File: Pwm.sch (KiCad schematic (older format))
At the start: 15 parts, among them P4 CONN_01X03, P5 CONN_01X03, P6 CONN_01X03, P7 CONN_01X03, U6 PCA9551

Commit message: version preliminar de la etapa de alimentacion
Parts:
- renumbered C7 to C21, C8 to C22, C9 to C23, C10 to C24, C11 to C25, P4 to P2, P5 to P3, P6 to P4, P7 to P5, R15 to R16, R16 to R17, R17 to R18, R18 to R19, R19 to R20, U6 to U9
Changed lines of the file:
@@
 LIBS:Sensores
 LIBS:Reles
+LIBS:Reguladores
+LIBS:Transistores
 LIBS:Wifi_PB-cache
 EELAYER 26 0
@@
 $Descr User 8268 5846
 encoding utf-8
-Sheet 7 11
+Sheet 7 15
 Title "Puerto de expansión para servomotores"
 Date "2017-01-15"
@@
 $EndDescr
 $Comp
-L CONN_01X03 P4
+L CONN_01X03 P2
 U 1 1 5794EA47
 P 6550 1350
-F 0 "P4" H 6628 1391 50  0000 L CNN
+F 0 "P2" H 6628 1391 50  0000 L CNN
 F 1 "CONN_01X03" H 6628 1300 50  0000 L CNN
 F 2 "Pin_Headers:Pin_Header_Straight_1x03_Pitch2.54mm" H 6550 1350 50  0001 C CNN
@@
 $EndComp
 $Comp
-L CONN_01X03 P5
+L CONN_01X03 P3
 U 1 1 5794EAA8
 P 6550 2050
-F 0 "P5" H 6628 2091 50  0000 L CNN
+F 0 "P3" H 6628 2091 50  0000 L CNN
 F 1 "CONN_01X03" H 6628 2000 50  0000 L CNN
 F 2 "Pin_Headers:Pin_Header_Straight_1x03_Pitch2.54mm" H 6550 2050 50  0001 C CNN
@@
 $EndComp
 $Comp
-L +5V #PWR026
+L +5V #PWR64
 U 1 1 5794EAD6
 P 6100 750
-F 0 "#PWR026" H 6100 600 50  0001 C CNN
+F 0 "#PWR64" H 6100 600 50  0001 C CNN
 F 1 "+5V" H 6115 923 50  0000 C CNN
 F 2 "" H 6100 750 50  0000 C CNN
@@
 $EndComp
 $Comp
-L GND #PWR027
+L GND #PWR65
 U 1 1 5794EAEE
 P 6200 3850
-F 0 "#PWR027" H 6200 3600 50  0001 C CNN
+F 0 "#PWR65" H 6200 3600 50  0001 C CNN
 F 1 "GND" H 6205 3677 50  0000 C CNN
 F 2 "" H 6200 3850 50  0000 C CNN
@@
 $EndBitmap
 $Comp
-L PCA9551 U6
+L PCA9551 U9
 U 1 1 586D5351
 P 1550 3800
-F 0 "U6" H 2100 3717 60  0000 C CNN
+F 0 "U9" H 2100 3717 60  0000 C CNN
 F 1 "PCA9551" H 2100 3597 79  0000 C CNN
 F 2 "Housings_SSOP:TSSOP-16_4.4x5mm_Pitch0.65mm" H 1550 3930 60  0001 C CNN
@@
 $EndComp
 $Comp
-L CONN_01X03 P6
+L CONN_01X03 P4
 U 1 1 586D53FE
 P 6550 2750
-F 0 "P6" H 6628 2791 50  0000 L CNN
+F 0 "P4" H 6628 2791 50  0000 L CNN
 F 1 "CONN_01X03" H 6628 2700 50  0000 L CNN
 F 2 "Pin_Headers:Pin_Header_Straight_1x03_Pitch2.54mm" H 6550 2750 50  0001 C CNN
@@
 $EndComp
 $Comp
-L CONN_01X03 P7
+L CONN_01X03 P5
 U 1 1 586D547C
 P 6550 3450
-F 0 "P7" H 6628 3491 50  0000 L CNN
+F 0 "P5" H 6628 3491 50  0000 L CNN
 F 1 "CONN_01X03" H 6628 3400 50  0000 L CNN
 F 2 "Pin_Headers:Pin_Header_Straight_1x03_Pitch2.54mm" H 6550 3450 50  0001 C CNN
@@
 	4100 1200 4100 1000
 $Comp
-L +5V #PWR028
+L +5V #PWR58
 U 1 1 586D5A4A
 P 4100 1000
-F 0 "#PWR028" H 4100 850 50  0001 C CNN
+F 0 "#PWR58" H 4100 850 50  0001 C CNN
 F 1 "+5V" H 4115 1173 50  0000 C CNN
 F 2 "" H 4100 1000 50  0000 C CNN
@@
 $EndComp
 $Comp
-L +5V #PWR029
+L +5V #PWR56
 U 1 1 586D5A77
 P 3750 1000
-F 0 "#PWR029" H 3750 850 50  0001 C CNN
+F 0 "#PWR56" H 3750 850 50  0001 C CNN
 F 1 "+5V" H 3765 1173 50  0000 C CNN
 F 2 "" H 3750 1000 50  0000 C CNN
@@
 $EndComp
 $Comp
-L +5V #PWR030
+L +5V #PWR54
 U 1 1 586D5A9D
 P 3400 1000
-F 0 "#PWR030" H 3400 850 50  0001 C CNN
+F 0 "#PWR54" H 3400 850 50  0001 C CNN
 F 1 "+5V" H 3415 1173 50  0000 C CNN
 F 2 "" H 3400 1000 50  0000 C CNN
@@
 $EndComp
 $Comp
-L +5V #PWR031
+L +5V #PWR52
 U 1 1 586D5AC3
 P 3050 1000
-F 0 "#PWR031" H 3050 850 50  0001 C CNN
+F 0 "#PWR52" H 3050 850 50  0001 C CNN
 F 1 "+5V" H 3065 1173 50  0000 C CNN
 F 2 "" H 3050 1000 50  0000 C CNN
@@
 $EndComp
 $Comp
-L GND #PWR032
+L GND #PWR53
 U 1 1 586D5AE2
 P 3050 1750
-F 0 "#PWR032" H 3050 1500 50  0001 C CNN
+F 0 "#PWR53" H 3050 1500 50  0001 C CNN
 F 1 "GND" H 3055 1577 50  0000 C CNN
 F 2 "" H 3050 1750 50  0000 C CNN
@@
 $EndComp
 $Comp
-L GND #PWR033
+L GND #PWR55
 U 1 1 586D5B0F
 P 3400 1750
-F 0 "#PWR033" H 3400 1500 50  0001 C CNN
+F 0 "#PWR55" H 3400 1500 50  0001 C CNN
 F 1 "GND" H 3405 1577 50  0000 C CNN
 F 2 "" H 3400 1750 50  0000 C CNN
@@
 $EndComp
 $Comp
-L GND #PWR034
+L GND #PWR57
 U 1 1 586D5B35
 P 3750 1750
-F 0 "#PWR034" H 3750 1500 50  0001 C CNN
+F 0 "#PWR57" H 3750 1500 50  0001 C CNN
 F 1 "GND" H 3755 1577 50  0000 C CNN
 F 2 "" H 3750 1750 50  0000 C CNN
@@
 $EndComp
 $Comp
-L GND #PWR035
+L GND #PWR59
 U 1 1 586D5B5B
 P 4100 1750
-F 0 "#PWR035" H 4100 1500 50  0001 C CNN
+F 0 "#PWR59" H 4100 1500 50  0001 C CNN
 F 1 "GND" H 4105 1577 50  0000 C CNN
 F 2 "" H 4100 1750 50  0000 C CNN
@@
 	2100 1450 2100 2350
 $Comp
-L GND #PWR036
+L GND #PWR51
 U 1 1 586D5DFC
 P 1750 2100
-F 0 "#PWR036" H 1750 1850 50  0001 C CNN
+F 0 "#PWR51" H 1750 1850 50  0001 C CNN
 F 1 "GND" H 1755 1927 50  0000 C CNN
 F 2 "" H 1750 2100 50  0000 C CNN
@@
 	1200 3250 1200 3950
 $Comp
-L GND #PWR037
+L GND #PWR49
 U 1 1 586D660B
 P 1200 3950
-F 0 "#PWR037" H 1200 3700 50  0001 C CNN
+F 0 "#PWR49" H 1200 3700 50  0001 C CNN
 F 1 "GND" H 1205 3777 50  0000 C CNN
 F 2 "" H 1200 3950 50  0000 C CNN
@@
 SERVO4
 $Comp
-L +5V #PWR038
+L +5V #PWR50
 U 1 1 586D839D
 P 1750 1300
-F 0 "#PWR038" H 1750 1150 50  0001 C CNN
+F 0 "#PWR50" H 1750 1150 50  0001 C CNN
 F 1 "+5V" H 1765 1473 50  0000 C CNN
 F 2 "" H 1750 1300 50  0000 C CNN
@@
 	5600 800  5600 850
 $Comp
-L +5V #PWR039
+L +5V #PWR63
 U 1 1 586FF4A2
 P 5600 2900
-F 0 "#PWR039" H 5600 2750 50  0001 C CNN
+F 0 "#PWR63" H 5600 2750 50  0001 C CNN
 F 1 "+5V" H 5615 3073 50  0000 C CNN
 F 2 "" H 5600 2900 50  0000 C CNN
@@
 	5600 2900 5600 2950
 $Comp
-L +5V #PWR040
+L +5V #PWR60
 U 1 1 586FF5CA
 P 5600 800
-F 0 "#PWR040" H 5600 650 50  0001 C CNN
+F 0 "#PWR60" H 5600 650 50  0001 C CNN
 F 1 "+5V" H 5615 973 50  0000 C CNN
 F 2 "" H 5600 800 50  0000 C CNN
@@
 $EndComp
 $Comp
-L +5V #PWR041
+L +5V #PWR62
 U 1 1 586FF689
 P 5600 2200
-F 0 "#PWR041" H 5600 2050 50  0001 C CNN
+F 0 "#PWR62" H 5600 2050 50  0001 C CNN
 F 1 "+5V" H 5615 2373 50  0000 C CNN
 F 2 "" H 5600 2200 50  0000 C CNN
@@
 $EndComp
 $Comp
-L +5V #PWR042
+L +5V #PWR61
 U 1 1 586FF6C1
 P 5600 1500
-F 0 "#PWR042" H 5600 1350 50  0001 C CNN
+F 0 "#PWR61" H 5600 1350 50  0001 C CNN
 F 1 "+5V" H 5615 1673 50  0000 C CNN
 F 2 "" H 5600 1500 50  0000 C CNN
@@
 	750  3050 1350 3050
 $Comp
-L +5V #PWR043
+L +5V #PWR48
 U 1 1 58700007
 P 750 2450
-F 0 "#PWR043" H 750 2300 50  0001 C CNN
+F 0 "#PWR48" H 750 2300 50  0001 C CNN
 F 1 "+5V" H 765 2623 50  0000 C CNN
 F 2 "" H 750 2450 50  0000 C CNN
@@
 	750  2450 750  2600
 $Comp
-L R R15
+L R R16
 U 1 1 58700C10
 P 750 2750
-F 0 "R15" V 850 2650 50  0000 L CNN
+F 0 "R16" V 850 2650 50  0000 L CNN
 F 1 "10K" V 750 2650 50  0000 L CNN
 F 2 "Resistencias:R_0805" V 680 2750 50  0001 C CNN
@@
 $EndComp
 $Comp
-L R R19
+L R R20
 U 1 1 58700D4F
 P 5600 3100
-F 0 "R19" V 5700 3000 50  0000 L CNN
+F 0 "R20" V 5700 3000 50  0000 L CNN
 F 1 "10K" V 5600 3000 50  0000 L CNN
 F 2 "Resistencias:R_0805" V 5530 3100 50  0001 C CNN
@@
 $EndComp
 $Comp
-L R R18
+L R R19
 U 1 1 58700ECF
 P 5600 2400
-F 0 "R18" V 5700 2300 50  0000 L CNN
+F 0 "R19" V 5700 2300 50  0000 L CNN
 F 1 "10K" V 5600 2300 50  0000 L CNN
 F 2 "Resistencias:R_0805" V 5530 2400 50  0001 C CNN
@@
 $EndComp
 $Comp
-L R R16
+L R R17
 U 1 1 5870102D
 P 5600 1000
-F 0 "R16" V 5700 900 50  0000 L CNN
+F 0 "R17" V 5700 900 50  0000 L CNN
 F 1 "10K" V 5600 900 50  0000 L CNN
 F 2 "Resistencias:R_0805" V 5530 1000 50  0001 C CNN
@@
 $EndComp
 $Comp
-L R R17
+L R R18
 U 1 1 5870117D
 P 5600 1700
-F 0 "R17" V 5700 1600 50  0000 L CNN
+F 0 "R18" V 5700 1600 50  0000 L CNN
 F 1 "10K" V 5600 1600 50  0000 L CNN
 F 2 "Resistencias:R_0805" V 5530 1700 50  0001 C CNN
@@
 	6350 1350 6100 1350
 $Comp
-L C C7
+L C C21
 U 1 1 58701807
 P 1750 1800
-F 0 "C7" H 1775 1900 50  0000 L CNN
+F 0 "C21" H 1775 1900 50  0000 L CNN
 F 1 "100n" H 1775 1700 50  0000 L CNN
 F 2 "Capacitors_SMD:C_0805" H 1788 1650 50  0001 C CNN
@@
 $EndComp
 $Comp
-L C C8
+L C C22
 U 1 1 58701B7E
 P 3050 1350
-F 0 "C8" H 3165 1396 50  0000 L CNN
+F 0 "C22" H 3165 1396 50  0000 L CNN
 F 1 "1u" H 3165 1305 50  0000 L CNN
 F 2 "Capacitors_SMD:C_0805" H 3088 1200 50  0001 C CNN
@@
 $EndComp
 $Comp
-L C C9
+L C C23
 U 1 1 58701CA2
 P 3400 1350
-F 0 "C9" H 3515 1396 50  0000 L CNN
+F 0 "C23" H 3515 1396 50  0000 L CNN
 F 1 "1u" H 3515 1305 50  0000 L CNN
 F 2 "Capacitors_SMD:C_0805" H 3438 1200 50  0001 C CNN
@@
 $EndComp
 $Comp
-L C C10
+L C C24
 U 1 1 58701CFA
 P 3750 1350
-F 0 "C10" H 3865 1396 50  0000 L CNN
+F 0 "C24" H 3865 1396 50  0000 L CNN
 F 1 "1u" H 3865 1305 50  0000 L CNN
 F 2 "Capacitors_SMD:C_0805" H 3788 1200 50  0001 C CNN
@@
 $EndComp
 $Comp
-L C C11
+L C C25
 U 1 1 58701D4D
 P 4100 1350
-F 0 "C11" H 4215 1396 50  0000 L CNN
+F 0 "C25" H 4215 1396 50  0000 L CNN
 F 1 "1u" H 4215 1305 50  0000 L CNN
 F 2 "Capacitors_SMD:C_0805" H 4138 1200 50  0001 C CNN

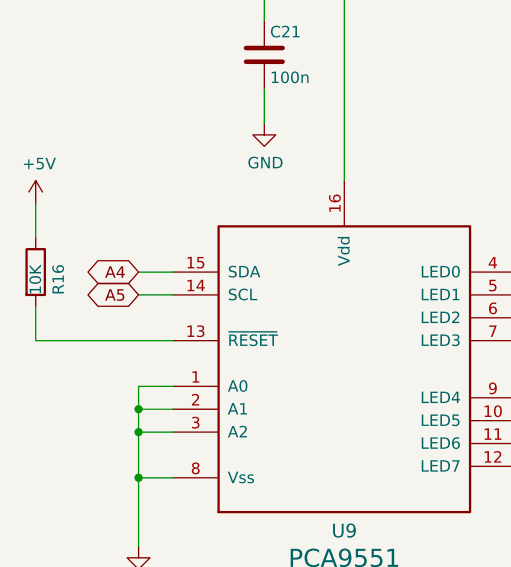
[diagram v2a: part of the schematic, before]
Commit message: cambiar ch340T por ch340g y añadir nc a pines
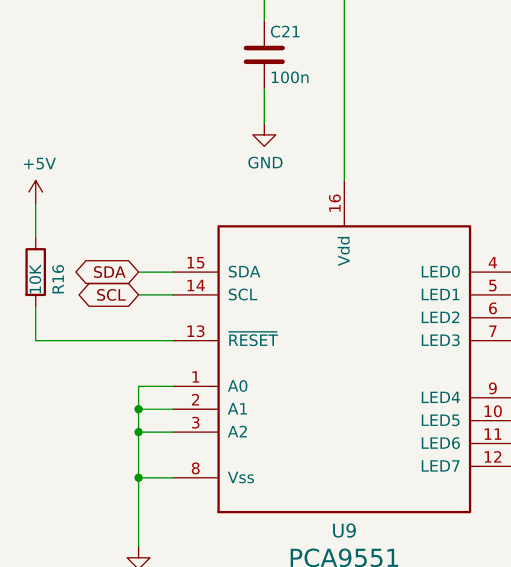
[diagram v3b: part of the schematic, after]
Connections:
- net A4 renamed SDA
- net A5 renamed SCL
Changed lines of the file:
@@
 $Descr User 8268 5846
 encoding utf-8
-Sheet 7 15
+Sheet 7 14
 Title "Puerto de expansión para servomotores"
 Date "2017-01-15"
@@
 $EndComp
 $Comp
-L +5V #PWR062
+L +5V #PWR070
 U 1 1 5794EAD6
 P 6100 750
-F 0 "#PWR062" H 6100 600 50  0001 C CNN
+F 0 "#PWR070" H 6100 600 50  0001 C CNN
 F 1 "+5V" H 6115 923 50  0000 C CNN
 F 2 "" H 6100 750 50  0000 C CNN
@@
 $EndComp
 $Comp
-L GND #PWR063
+L GND #PWR071
 U 1 1 5794EAEE
 P 6200 3850
-F 0 "#PWR063" H 6200 3600 50  0001 C CNN
+F 0 "#PWR071" H 6200 3600 50  0001 C CNN
 F 1 "GND" H 6205 3677 50  0000 C CNN
 F 2 "" H 6200 3850 50  0000 C CNN
@@
 	4100 1200 4100 1000
 $Comp
-L +5V #PWR064
+L +5V #PWR072
 U 1 1 586D5A4A
 P 4100 1000
-F 0 "#PWR064" H 4100 850 50  0001 C CNN
+F 0 "#PWR072" H 4100 850 50  0001 C CNN
 F 1 "+5V" H 4115 1173 50  0000 C CNN
 F 2 "" H 4100 1000 50  0000 C CNN
@@
 $EndComp
 $Comp
-L +5V #PWR065
+L +5V #PWR073
 U 1 1 586D5A77
 P 3750 1000
-F 0 "#PWR065" H 3750 850 50  0001 C CNN
+F 0 "#PWR073" H 3750 850 50  0001 C CNN
 F 1 "+5V" H 3765 1173 50  0000 C CNN
 F 2 "" H 3750 1000 50  0000 C CNN
@@
 $EndComp
 $Comp
-L +5V #PWR066
+L +5V #PWR074
 U 1 1 586D5A9D
 P 3400 1000
-F 0 "#PWR066" H 3400 850 50  0001 C CNN
+F 0 "#PWR074" H 3400 850 50  0001 C CNN
 F 1 "+5V" H 3415 1173 50  0000 C CNN
 F 2 "" H 3400 1000 50  0000 C CNN
@@
 $EndComp
 $Comp
-L +5V #PWR067
+L +5V #PWR075
 U 1 1 586D5AC3
 P 3050 1000
-F 0 "#PWR067" H 3050 850 50  0001 C CNN
+F 0 "#PWR075" H 3050 850 50  0001 C CNN
 F 1 "+5V" H 3065 1173 50  0000 C CNN
 F 2 "" H 3050 1000 50  0000 C CNN
@@
 $EndComp
 $Comp
-L GND #PWR068
+L GND #PWR076
 U 1 1 586D5AE2
 P 3050 1750
-F 0 "#PWR068" H 3050 1500 50  0001 C CNN
+F 0 "#PWR076" H 3050 1500 50  0001 C CNN
 F 1 "GND" H 3055 1577 50  0000 C CNN
 F 2 "" H 3050 1750 50  0000 C CNN
@@
 $EndComp
 $Comp
-L GND #PWR069
+L GND #PWR077
 U 1 1 586D5B0F
 P 3400 1750
-F 0 "#PWR069" H 3400 1500 50  0001 C CNN
+F 0 "#PWR077" H 3400 1500 50  0001 C CNN
 F 1 "GND" H 3405 1577 50  0000 C CNN
 F 2 "" H 3400 1750 50  0000 C CNN
@@
 $EndComp
 $Comp
-L GND #PWR070
+L GND #PWR078
 U 1 1 586D5B35
 P 3750 1750
-F 0 "#PWR070" H 3750 1500 50  0001 C CNN
+F 0 "#PWR078" H 3750 1500 50  0001 C CNN
 F 1 "GND" H 3755 1577 50  0000 C CNN
 F 2 "" H 3750 1750 50  0000 C CNN
@@
 $EndComp
 $Comp
-L GND #PWR071
+L GND #PWR079
 U 1 1 586D5B5B
 P 4100 1750
-F 0 "#PWR071" H 4100 1500 50  0001 C CNN
+F 0 "#PWR079" H 4100 1500 50  0001 C CNN
 F 1 "GND" H 4105 1577 50  0000 C CNN
 F 2 "" H 4100 1750 50  0000 C CNN
@@
 	2100 1450 2100 2350
 $Comp
-L GND #PWR072
+L GND #PWR080
 U 1 1 586D5DFC
 P 1750 2100
-F 0 "#PWR072" H 1750 1850 50  0001 C CNN
+F 0 "#PWR080" H 1750 1850 50  0001 C CNN
 F 1 "GND" H 1755 1927 50  0000 C CNN
 F 2 "" H 1750 2100 50  0000 C CNN
@@
 	1200 3250 1200 3950
 $Comp
-L GND #PWR073
+L GND #PWR081
 U 1 1 586D660B
 P 1200 3950
-F 0 "#PWR073" H 1200 3700 50  0001 C CNN
+F 0 "#PWR081" H 1200 3700 50  0001 C CNN
 F 1 "GND" H 1205 3777 50  0000 C CNN
 F 2 "" H 1200 3950 50  0000 C CNN
@@
 	1350 2750 1200 2750
 Text GLabel 1200 2750 0    50   BiDi ~ 0
-A4
+SDA
 Wire Wire Line
 	1200 2850 1350 2850
 Text GLabel 1200 2850 0    50   BiDi ~ 0
-A5
+SCL
 Text GLabel 3400 3300 2    50   Output ~ 0
 LED_RED
@@
 SERVO4
 $Comp
-L +5V #PWR074
+L +5V #PWR082
 U 1 1 586D839D
 P 1750 1300
-F 0 "#PWR074" H 1750 1150 50  0001 C CNN
+F 0 "#PWR082" H 1750 1150 50  0001 C CNN
 F 1 "+5V" H 1765 1473 50  0000 C CNN
 F 2 "" H 1750 1300 50  0000 C CNN
@@
 	5600 800  5600 850
 $Comp
-L +5V #PWR075
+L +5V #PWR083
 U 1 1 586FF4A2
 P 5600 2900
-F 0 "#PWR075" H 5600 2750 50  0001 C CNN
+F 0 "#PWR083" H 5600 2750 50  0001 C CNN
 F 1 "+5V" H 5615 3073 50  0000 C CNN
 F 2 "" H 5600 2900 50  0000 C CNN
@@
 	5600 2900 5600 2950
 $Comp
-L +5V #PWR076
+L +5V #PWR084
 U 1 1 586FF5CA
 P 5600 800
-F 0 "#PWR076" H 5600 650 50  0001 C CNN
+F 0 "#PWR084" H 5600 650 50  0001 C CNN
 F 1 "+5V" H 5615 973 50  0000 C CNN
 F 2 "" H 5600 800 50  0000 C CNN
@@
 $EndComp
 $Comp
-L +5V #PWR077
+L +5V #PWR085
 U 1 1 586FF689
 P 5600 2200
-F 0 "#PWR077" H 5600 2050 50  0001 C CNN
+F 0 "#PWR085" H 5600 2050 50  0001 C CNN
 F 1 "+5V" H 5615 2373 50  0000 C CNN
 F 2 "" H 5600 2200 50  0000 C CNN
@@
 $EndComp
 $Comp
-L +5V #PWR078
+L +5V #PWR086
 U 1 1 586FF6C1
 P 5600 1500
-F 0 "#PWR078" H 5600 1350 50  0001 C CNN
+F 0 "#PWR086" H 5600 1350 50  0001 C CNN
 F 1 "+5V" H 5615 1673 50  0000 C CNN
 F 2 "" H 5600 1500 50  0000 C CNN
@@
 	750  3050 1350 3050
 $Comp
-L +5V #PWR079
+L +5V #PWR087
 U 1 1 58700007
 P 750 2450
-F 0 "#PWR079" H 750 2300 50  0001 C CNN
+F 0 "#PWR087" H 750 2300 50  0001 C CNN
 F 1 "+5V" H 765 2623 50  0000 C CNN
 F 2 "" H 750 2450 50  0000 C CNN

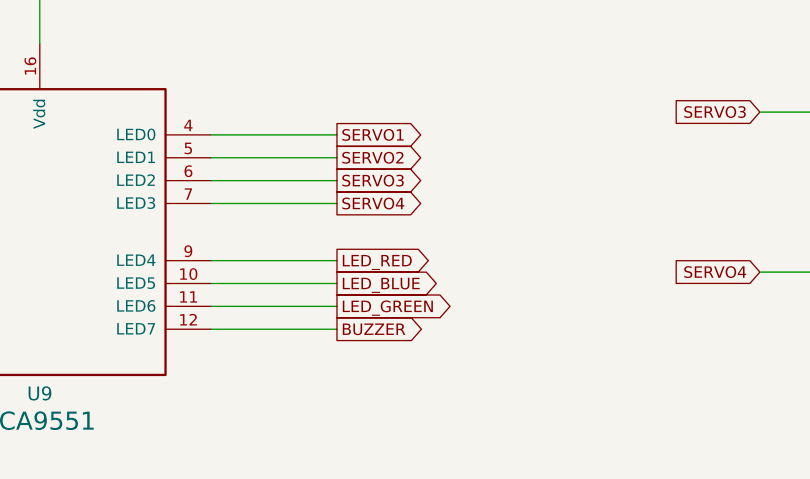
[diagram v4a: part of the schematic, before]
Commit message: modificado conexion led rgb para mejorar trazado
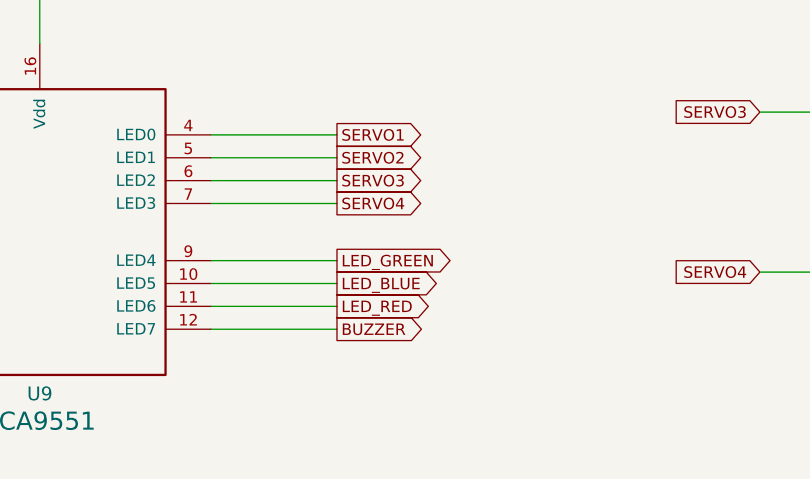
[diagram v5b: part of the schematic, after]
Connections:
- net LED_GREEN: now also U9.9 (LED4); no longer U9.11 (LED6)
- net LED_RED: now also U9.11 (LED6); no longer U9.9 (LED4)
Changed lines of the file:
@@
 Text GLabel 1200 2850 0    50   BiDi ~ 0
 SCL
+Text GLabel 3400 3500 2    50   Output ~ 0
+LED_RED
 Text GLabel 3400 3300 2    50   Output ~ 0
-LED_RED
-Text GLabel 3400 3500 2    50   Output ~ 0
 LED_GREEN
 Text GLabel 3400 3400 2    50   Output ~ 0
